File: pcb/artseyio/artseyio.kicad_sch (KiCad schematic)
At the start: 14 parts, among them SW1 SW_MEC_5G, SW2 SW_MEC_5G, SW3 SW_MEC_5G, SW4 SW_MEC_5G, SW5 SW_MEC_5G, SW6 SW_MEC_5G, SW7 SW_MEC_5G, SW8 SW_MEC_5G, U1 RP2040-Zero, U2 mini_esp32

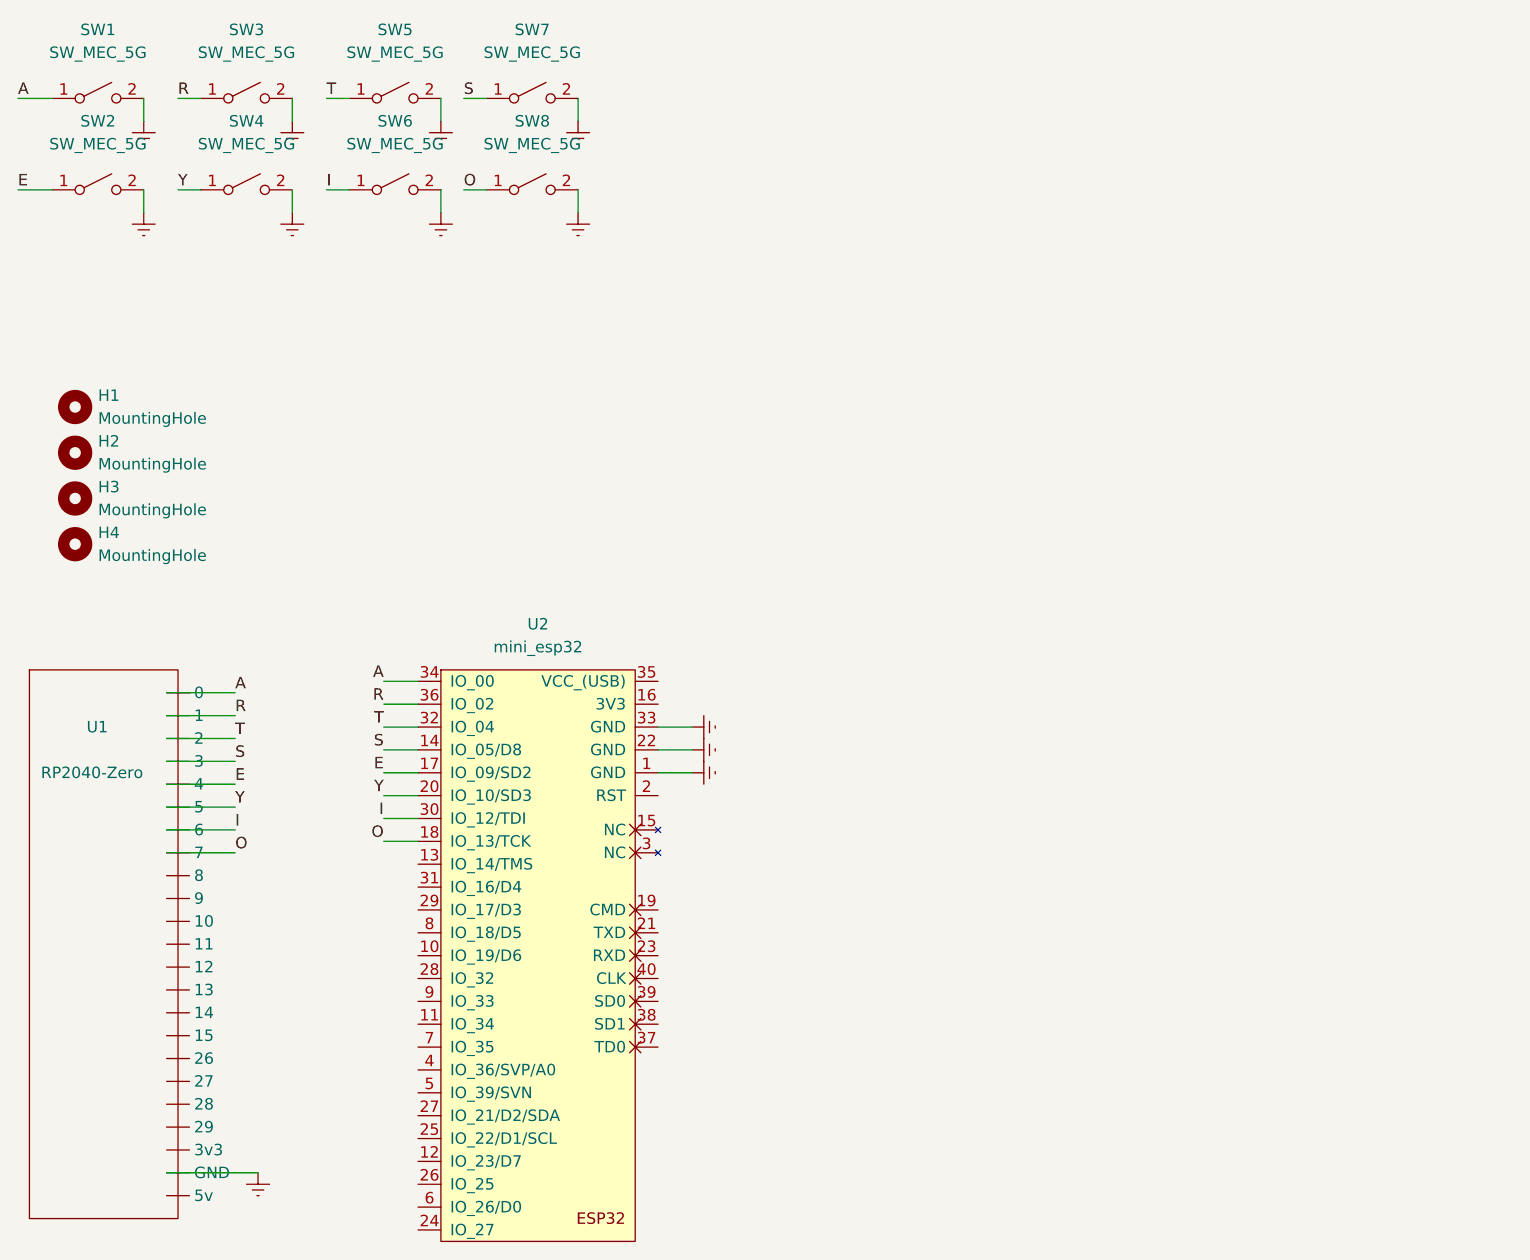
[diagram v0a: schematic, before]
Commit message: Updated schematic to include  a CH552 with builtin USB-C port.
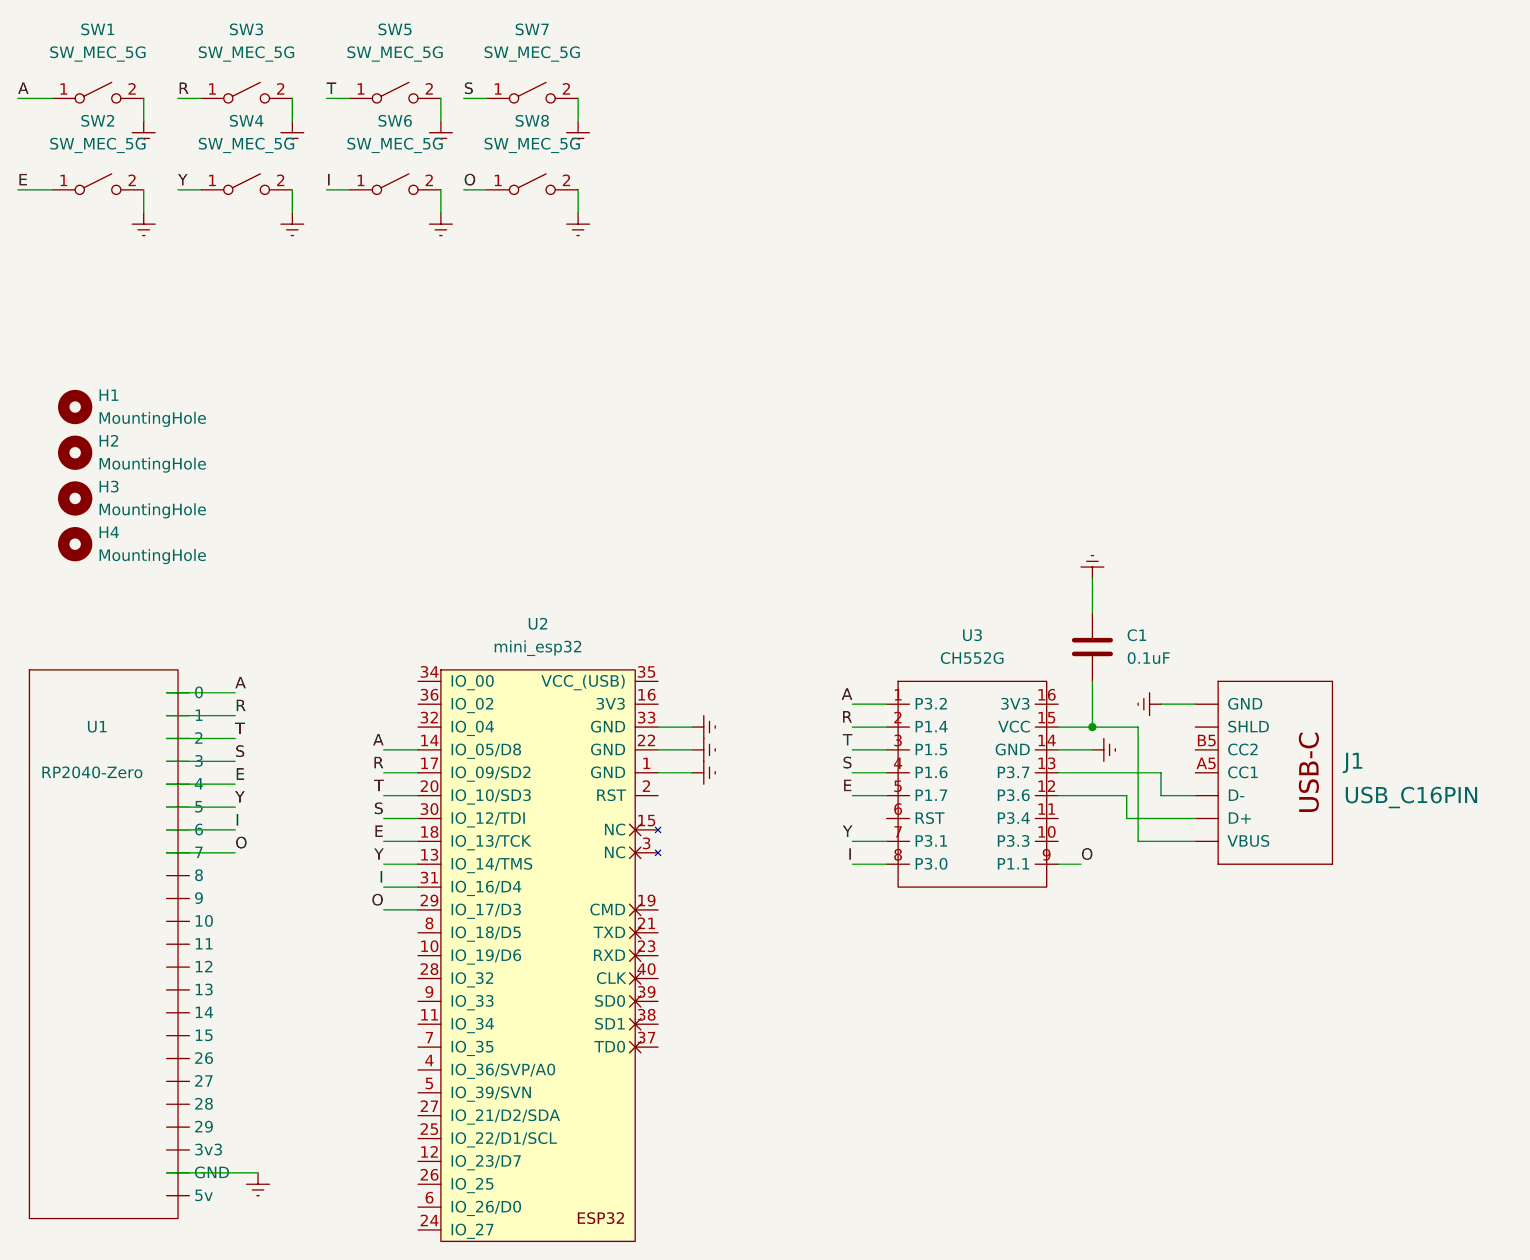
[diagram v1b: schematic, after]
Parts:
- added C1: 0.1uF, Capacitor_SMD:C_0805_2012Metric_Pad1.18x1.45mm_HandSolder, symbol Device:C
- added J1: USB_C16PIN, USB-C:USB-C-COM-15111, symbol USB-C:USB_C16PIN
- added U3: CH552G, CH552G:CH552G, symbol CH552G:CH552G
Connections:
- net A: now also U2.14 (IO_05/D8), U3.1 (P3.2); no longer U2.34 (IO_00)
- net E: now also U2.18 (IO_13/TCK), U3.5 (P1.7); no longer U2.17 (IO_09/SD2)
- net Earth: now also C1.1, J1.GND, J1.GND2 (GND), U3.14 (GND)
- net I: now also U2.31 (IO_16/D4), U3.8 (P3.0); no longer U2.30 (IO_12/TDI)
- net O: now also U2.29 (IO_17/D3), U3.9 (P1.1); no longer U2.18 (IO_13/TCK)
- net R: now also U2.17 (IO_09/SD2), U3.2 (P1.4); no longer U2.36 (IO_02)
- net S: now also U2.30 (IO_12/TDI), U3.4 (P1.6); no longer U2.14 (IO_05/D8)
- net T: now also U2.20 (IO_10/SD3), U3.3 (P1.5); no longer U2.32 (IO_04)
- net Y: now also U2.13 (IO_14/TMS), U3.7 (P3.1); no longer U2.20 (IO_10/SD3)
- new net: J1.A6 (D+), J1.B6 (D+), U3.12 (P3.6)
- new net: J1.A7 (D-), J1.B7 (D-), U3.13 (P3.7)
- new net: J1.SHLD1 (SHLD), J1.SHLD2 (SHLD), J1.SHLD3 (SHLD), J1.SHLD4 (SHLD), J1.SHLD5 (SHLD), J1.SHLD6 (SHLD), J1.SHLD7 (SHLD), J1.SHLD8 (SHLD)
- new net: C1.2, J1.VBUS1 (VBUS), J1.VBUS2 (VBUS), U3.15 (VCC)

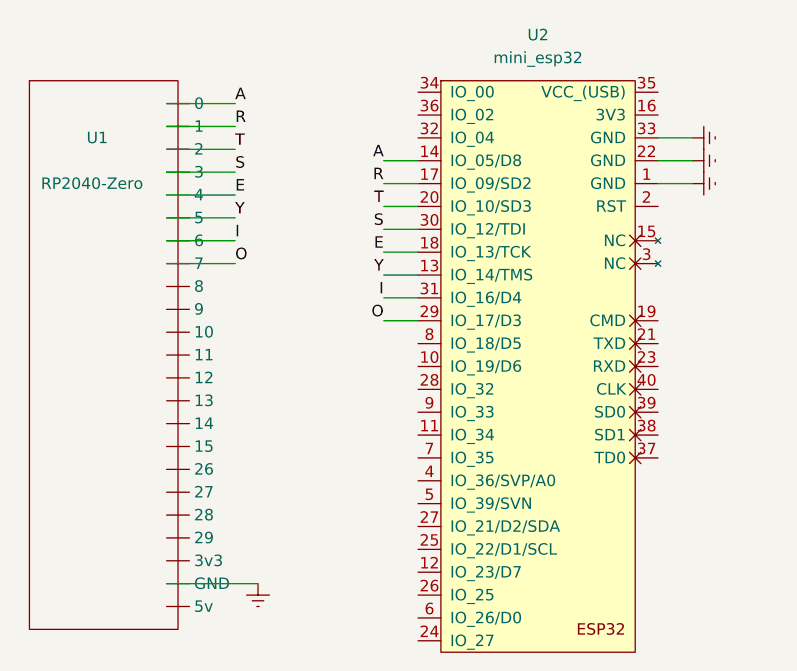
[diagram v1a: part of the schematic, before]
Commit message: Updated the footprint shape and updated the ESP32 pinout.
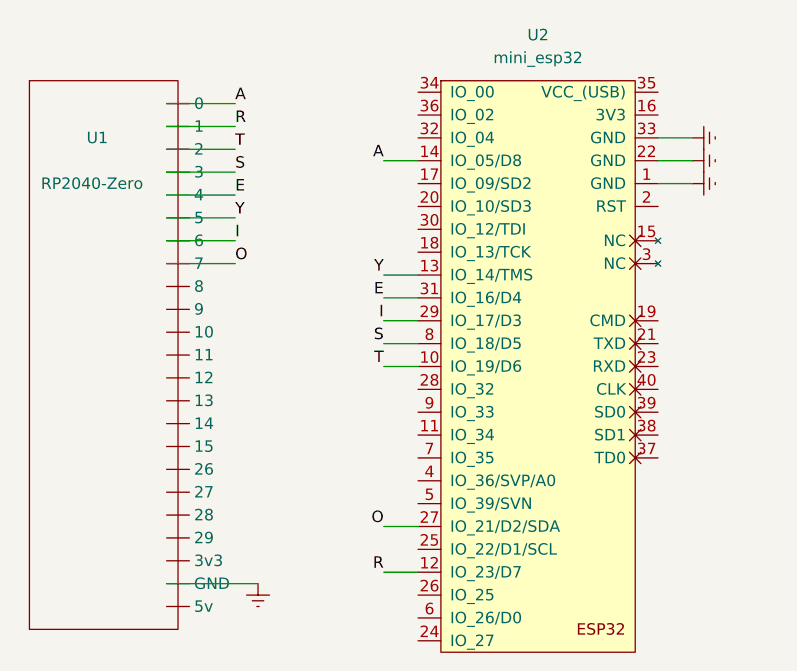
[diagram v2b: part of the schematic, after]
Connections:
- net E: now also U2.31 (IO_16/D4); no longer U2.18 (IO_13/TCK)
- net I: now also U2.29 (IO_17/D3); no longer U2.31 (IO_16/D4)
- net O: now also U2.27 (IO_21/D2/SDA); no longer U2.29 (IO_17/D3)
- net R: now also U2.12 (IO_23/D7); no longer U2.17 (IO_09/SD2)
- net S: now also U2.8 (IO_18/D5); no longer U2.30 (IO_12/TDI)
- net T: now also U2.10 (IO_19/D6); no longer U2.20 (IO_10/SD3)

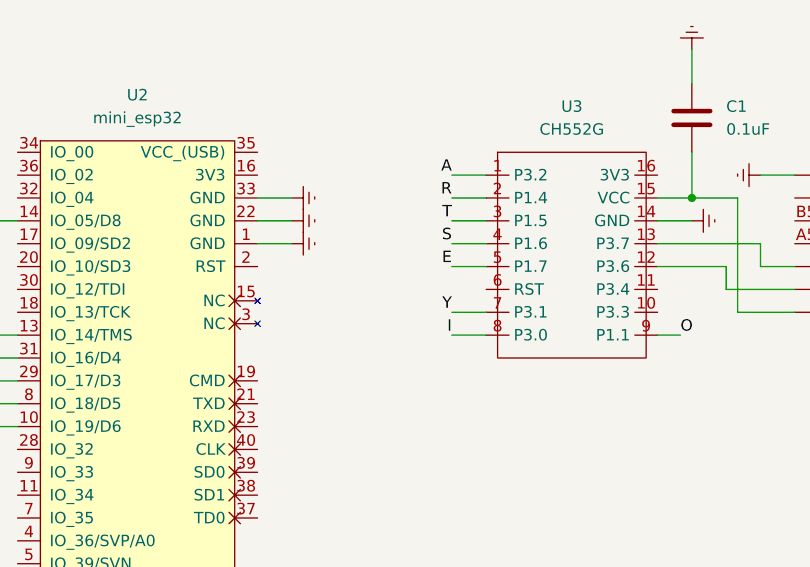
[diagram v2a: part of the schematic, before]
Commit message: Added reset jumpers for CH552G
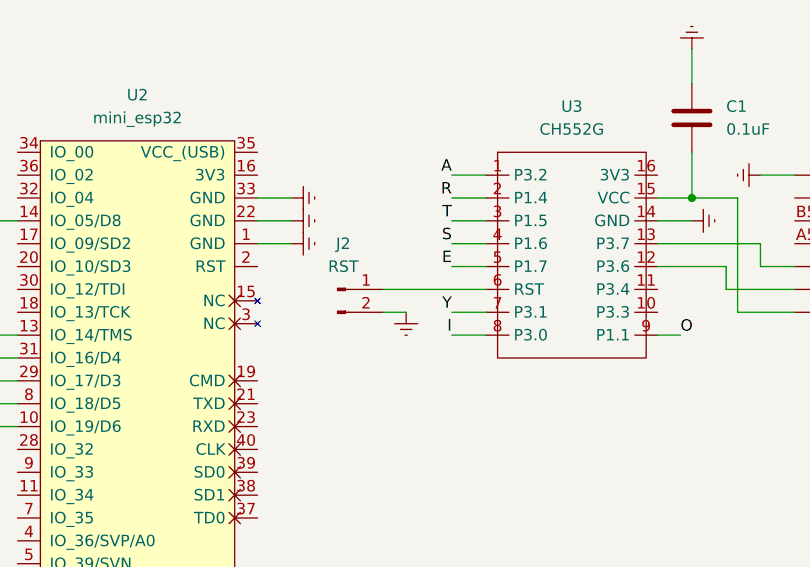
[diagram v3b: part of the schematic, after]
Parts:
- added J2: RST, Connector_PinHeader_2.54mm:PinHeader_1x02_P2.54mm_Vertical, symbol Connector:Conn_01x02_Male
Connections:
- net Earth: now also J2.2 (Pin_2)
- net at U3.6 (RST): now also J2.1 (Pin_1)
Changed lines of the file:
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@@
+    (stroke (width 0) (type default) (color 0 0 0 0))
+  )
+  (wire (pts (xy 171.45 124.46) (xy 173.99 124.46))
     (stroke (width 0) (type default) (color 0 0 0 0))
   )
@@
     (stroke (width 0) (type default) (color 0 0 0 0))
   )
+  (wire (pts (xy 171.45 121.92) (xy 182.88 121.92))
+    (stroke (width 0) (type default) (color 0 0 0 0))
+  )
   (wire (pts (xy 127 160.02) (xy 130.81 160.02))
     (stroke (width 0) (type default) (color 0 0 0 0))
@@
   (label "E" (at 127 129.54 180)
     (effects (font (size 1.27 1.27)) (justify right bottom))
+  )
+  (symbol (lib_id "Connector:Conn_01x02_Male") (at 166.37 121.92 0) (unit 1)
+    (in_bom yes) (on_board yes) (fields_autoplaced)
+    (property "Reference" "J2" (id 0) (at 167.005 116.84 0))
+    (property "Value" "RST" (id 1) (at 167.005 119.38 0))
+    (property "Footprint" "Connector_PinHeader_2.54mm:PinHeader_1x02_P2.54mm_Vertical" (id 2) (at 166.37 121.92 0)
+      (effects (font (size 1.27 1.27)) hide)
+    )
+    (property "Datasheet" "~" (id 3) (at 166.37 121.92 0)
+      (effects (font (size 1.27 1.27)) hide)
+    )
+    (pin "1")
+    (pin "2")
   )
   (symbol (lib_id "power:Earth") (at 113.03 161.29 0) (unit 1)
@@
       (effects (font (size 1.27 1.27)) hide)
     )
+  )
+  (symbol (lib_id "power:Earth") (at 173.99 124.46 0) (unit 1)
+    (in_bom yes) (on_board yes) (fields_autoplaced)
+    (property "Reference" "#PWR0113" (id 0) (at 173.99 130.81 0)
+      (effects (font (size 1.27 1.27)) hide)
+    )
+    (property "Value" "Earth" (id 1) (at 173.99 128.27 0)
+      (effects (font (size 1.27 1.27)) hide)
+    )
+    (property "Footprint" "" (id 2) (at 173.99 124.46 0)
+      (effects (font (size 1.27 1.27)) hide)
+    )
+    (property "Datasheet" "~" (id 3) (at 173.99 124.46 0)
+      (effects (font (size 1.27 1.27)) hide)
+    )
+    (pin "1")
   )
   (symbol (lib_id "power:Earth") (at 133.35 54.61 0) (unit 1)
@@
       (reference "#PWR0112") (unit 1) (value "Earth") (footprint "")
     )
+    (path "/b5a059b1-9dd6-4ed3-b2e0-e508763eb294"
+      (reference "#PWR0113") (unit 1) (value "Earth") (footprint "")
+    )
     (path "/3a15664c-0481-4447-bd31-45cdb071e406"
       (reference "C1") (unit 1) (value "0.1uF") (footprint "Capacitor_SMD:C_0805_2012Metric_Pad1.18x1.45mm_HandSolder")
@@
       (reference "J1") (unit 1) (value "USB_C16PIN") (footprint "USB-C:USB-C-COM-15111")
     )
+    (path "/00867e46-1312-47ae-9020-9b2d27765335"
+      (reference "J2") (unit 1) (value "RST") (footprint "Connector_PinHeader_2.54mm:PinHeader_1x02_P2.54mm_Vertical")
+    )
     (path "/cea2e4e4-36b1-428b-9719-886f80f64285"

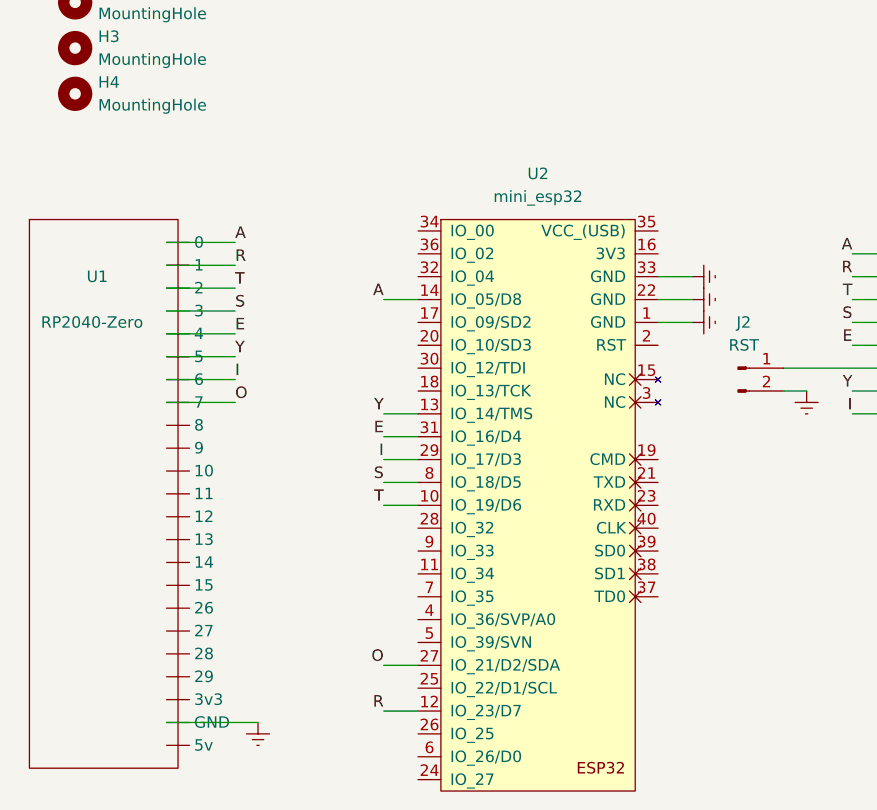
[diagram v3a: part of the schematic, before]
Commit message: Updated to remove RP2040-Zero and ESP32.
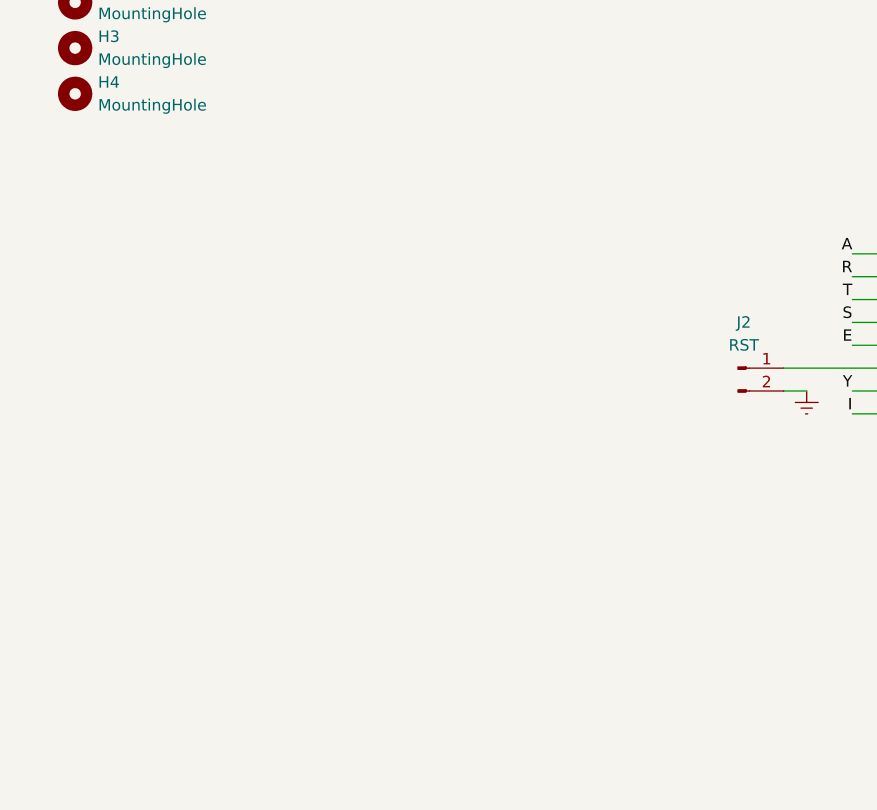
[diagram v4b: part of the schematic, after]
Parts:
- removed U1: RP2040-Zero, Andrews-Custom:RP2040-Zero, symbol Andrews-symbols:RP2040-Zero
- removed U2: mini_esp32, ESP32 Mini:ESP32_mini, symbol ESP32 Mini:mini_esp32

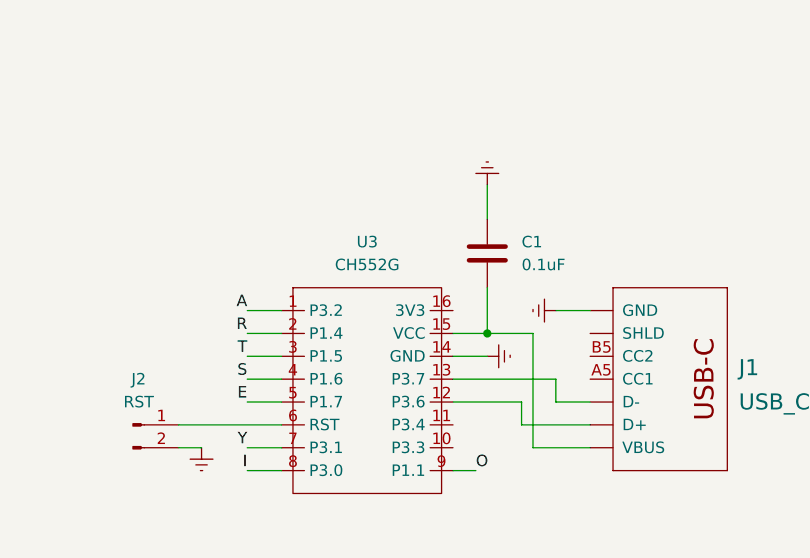
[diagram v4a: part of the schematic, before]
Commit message: Added in some missing features to make programming it easier, handle CC lines on USB-C.
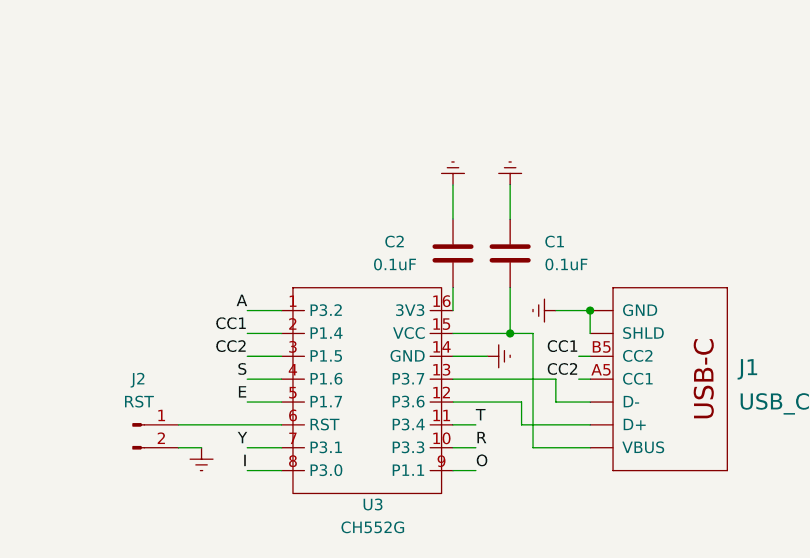
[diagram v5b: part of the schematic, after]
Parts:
- added C2: 0.1uF, Capacitor_SMD:C_0805_2012Metric_Pad1.18x1.45mm_HandSolder, symbol Device:C
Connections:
- net Earth: now also J1.SHLD1 (SHLD), J1.SHLD2 (SHLD), J1.SHLD3 (SHLD), J1.SHLD4 (SHLD), J1.SHLD5 (SHLD), J1.SHLD6 (SHLD), J1.SHLD7 (SHLD), J1.SHLD8 (SHLD), C2.1
- net R: now also U3.10 (P3.3); no longer U3.2 (P1.4)
- net T: now also U3.11 (P3.4); no longer U3.3 (P1.5)
- net CC2: now reaches J1.A5 (CC1)
- net CC2: now also U3.3 (P1.5)
- net CC1: now reaches J1.B5 (CC2)
- net CC1: now also U3.2 (P1.4)
- net at U3.16 (3V3): now also C2.2
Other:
- moved on the sheet: C1
